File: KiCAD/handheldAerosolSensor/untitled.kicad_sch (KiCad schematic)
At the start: 17 parts, among them J201 PWR-OUT, J202 Ext.Sw, Q201 AO3401, Q202 BC848, Q203 BC848, SW201 PWR, U202 Mini DC-DC Convertor

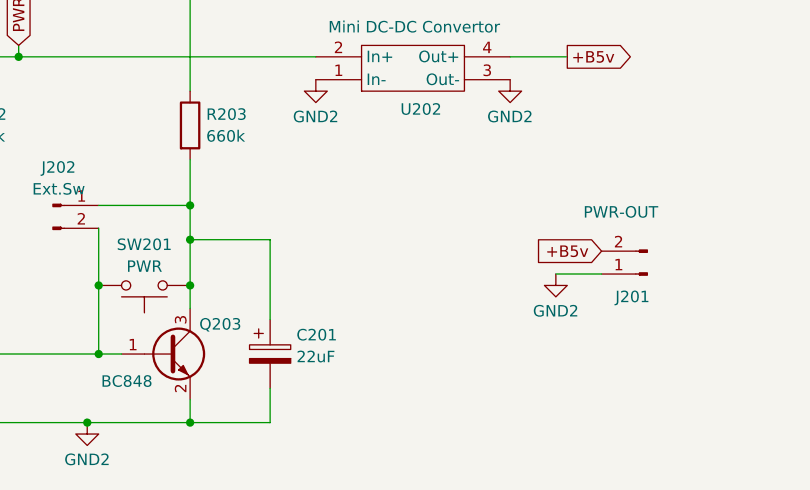
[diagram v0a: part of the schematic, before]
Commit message: Add power indicator LED (D201) with supporting components to the PCB design: - Add 1206 SMD power LED with current limiting resistor - Add new nets for LED connections (Net-(C201-Pad1), Net-(D201-A)) - Update PCB plot parameters (layer selection and drill shape settings) - Adjust component placement for R6 resistor - Update design date to 2026-02-15
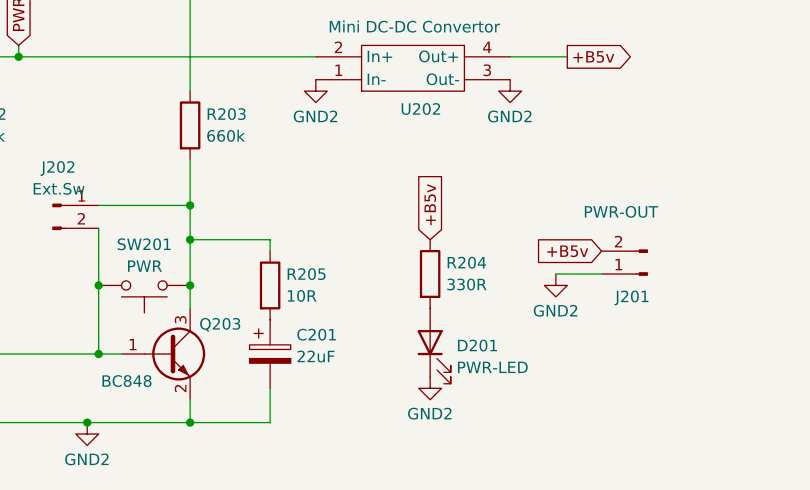
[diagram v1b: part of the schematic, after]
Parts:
- added D201: PWR-LED, LED_SMD:LED_1206_3216Metric_Pad1.42x1.75mm_HandSolder, symbol Device:LED
- added R204: 330R, Resistor_SMD:R_1206_3216Metric_Pad1.30x1.75mm_HandSolder, symbol Device:R
- added R205: 10R, Resistor_SMD:R_1206_3216Metric_Pad1.30x1.75mm_HandSolder, symbol Device:R
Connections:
- net +B5v: now also R204.1
- net GND2: now also D201.1 (K)
- net at J202.1 (Pin_1), Q203.3 (C), R203.2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: now also R205.1; no longer C201.1
- new net: D201.2 (A), R204.2
- new net: C201.1, R205.2
